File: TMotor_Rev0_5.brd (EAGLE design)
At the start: 106.7 x 79.4 mm, 105 parts, among them U1 INA125U, U10 DEV-16771, U2 INA125U, U3 INA125U, U4 INA125U, U5 SN65HVD230MDREP, U6 2SJ305TE85LF, U7 2SJ305TE85LF, U8 2SJ305TE85LF, U9 2SJ305TE85LF

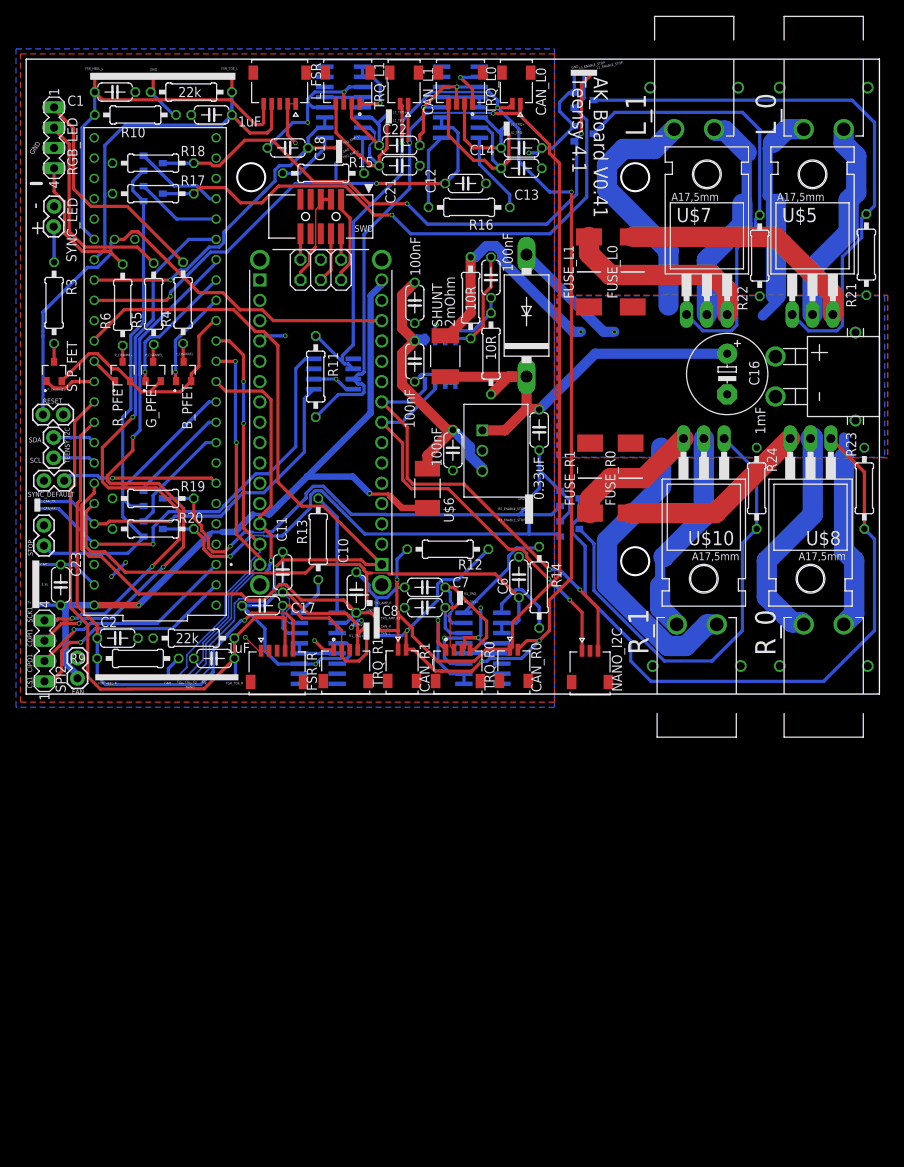
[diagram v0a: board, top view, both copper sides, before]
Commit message: Removed Power FETS, power FET supporting hardware, and SWD IO for nano
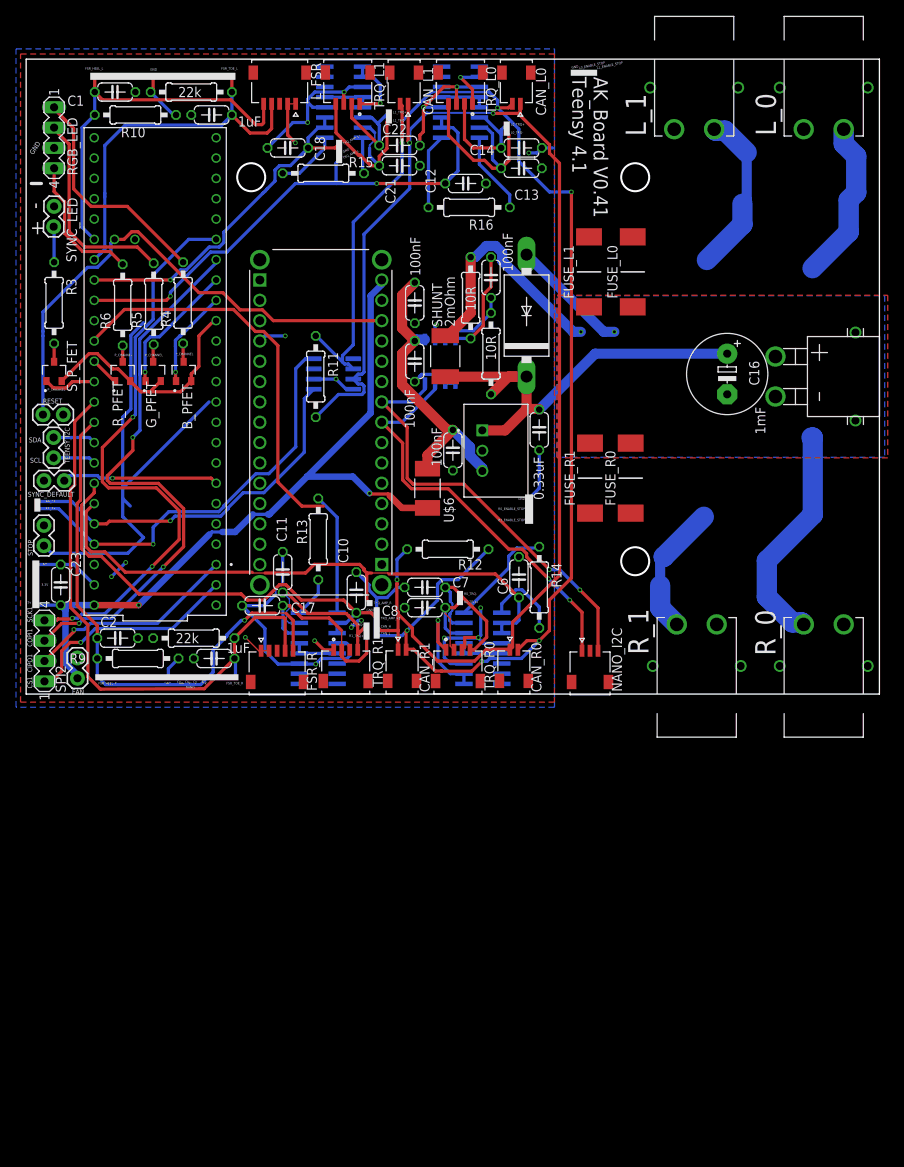
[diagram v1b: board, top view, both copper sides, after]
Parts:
- removed POGO: (no value), pinhead:2X03
- removed R17, R18: 1K, rcl:0207/10
- removed R19, R20: 1k, rcl:0207/10
- removed R21, R22, R23, R24: 10K, rcl:0207/10
- removed SWD: 20317, microbuilder:2X05_1.27MM_BOX_POSTS
- removed U$1, U$2, U$3, U$4: SSM3K329R, SnapEDA-Library:TRANS_SSM3J325F,LF
- removed U$10, U$5, U$7, U$8: FQP12P20, SnapEDA-Library:TO220
- removed U6, U7, U8, U9: 2SJ305TE85LF, 2SJ305TE85LF:TRANS_SSM3J325F,LF
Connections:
- removed net L0_ENABLE_STOP: R17.2, U$1.1, U6.3
- removed net L1_ENABLE_STOP: R18.2, U$2.1, U7.3
- removed net L_0_ENABLE: U10.28, U6.2
- removed net L_1_ENABLE: U10.29, U7.2
- removed net MISO: U10.11, USB.B15
- removed net MOSI: U10.12, USB.B14
- removed net N$43: R21.2, U$1.3, U$5.1
- removed net N$46: FUSE_R1.2, U$10.3
- removed net N$47: R23.2, U$3.3, U$8.1
- removed net N$48: R22.2, U$2.3, U$7.1
- removed net N$49: R24.2, U$10.1, U$4.3
- removed net N$50: FUSE_R0.2, U$8.3
- removed net N$51: FUSE_L1.2, U$7.3
- removed net N$52: FUSE_L0.2, U$5.3
- removed net NANO_CS: U10.10, USB.B13
- removed net NRESET: POGO.5, SWD.10
- removed net R0_ENABLE_STOP: R19.2, U$3.1, U8.3
- removed net R1_ENABLE_STOP: R20.2, U$4.1, U9.3
- removed net R_0_ENABLE: U10.8, U8.2
- removed net R_1_ENABLE: U10.7, U9.2
- removed net SW3.3V: POGO.2, SWD.1
- removed net SWCLK: POGO.4, SWD.4
- removed net SWDIO: POGO.1, SWD.2
- removed net SWGND: POGO.6, SWD.3, SWD.5
- net GND: no longer R17.1, R18.1, R19.1, R20.1, U$1.2, U$2.2, U$3.2, U$4.2
- net N$53: now also FUSE_L0.2; no longer U$5.2
- net N$54: now also FUSE_L1.2; no longer U$7.2
- net N$55: now also FUSE_R0.2; no longer U$8.2
- net N$56: now also FUSE_R1.2; no longer U$10.2
- net SCK: no longer USB.A1
- net STOP: no longer U10.9, U6.1, U7.1, U8.1, U9.1
- net VCC: no longer R21.1, R22.1, R23.1, R24.1
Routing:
- net GND: track 306.0 -> 164.2 mm, vias 24 -> 23
- net N$47: track 84.1 -> 0.00 mm
- net L0_ENABLE_STOP: track 76.0 -> 0.00 mm, vias 2 -> 0
- net L1_ENABLE_STOP: track 75.4 -> 0.00 mm, vias 3 -> 0
- net N$43: track 70.7 -> 0.00 mm
- net R0_ENABLE_STOP: track 62.2 -> 0.00 mm, vias 2 -> 0
- net R1_ENABLE_STOP: track 60.3 -> 0.00 mm, vias 2 -> 0
- net N$49: track 58.7 -> 0.00 mm
- net N$48: track 55.8 -> 0.00 mm
- net MOSI: track 49.6 -> 0.00 mm, vias 3 -> 0
- net NANO_CS: track 48.4 -> 0.00 mm, vias 2 -> 0
- net MISO: track 47.2 -> 0.00 mm, vias 3 -> 0
- net SCK: track 94.7 -> 50.6 mm, vias 2 -> 0
- net N$52: track 30.5 -> 0.00 mm
- net N$51: track 24.3 -> 0.00 mm
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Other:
- board text added: "3. Remove SPI, replace with Serial and I2C between boards"
- board text removed: "3. Figure out how to keep SPI from preventing flashing"

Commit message: Added serial connection between nano and teensy
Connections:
- new net NANO_RX: U10.35, USB.B2
- new net NANO_TX: U10.34, USB.B1
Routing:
- net N$54: track 20.8 -> 0.00 mm
- net N$53: track 20.3 -> 0.00 mm
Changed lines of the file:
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@@
 <wire x1="47.3475" y1="75.368" x2="63.54" y2="75.368" width="0" layer="19" extent="1-1"/>
 <wire x1="32.14" y1="73.025" x2="47.3475" y2="75.368" width="0" layer="19" extent="16-16"/>
-<wire x1="30.7975" y1="70.485" x2="29.1747" y2="72.4027875" width="0" layer="19" extent="1-1"/>
-<wire x1="23.8125" y1="68.58" x2="29.1747" y2="72.4027875" width="0" layer="19" extent="1-1"/>
-<wire x1="15.5575" y1="70.8025" x2="23.8125" y2="68.58" width="0" layer="19" extent="1-1"/>
-<wire x1="15.5575" y1="73.3425" x2="15.5575" y2="70.8025" width="0" layer="19" extent="1-1"/>
-<wire x1="8.3947" y1="80.645" x2="16.002" y2="78.105" width="0" layer="19" extent="16-16"/>
-<wire x1="5.461" y1="72.517" x2="1.524" y2="76.2" width="0" layer="19" extent="1-1"/>
-<wire x1="28.8925" y1="59.69" x2="23.8125" y2="68.58" width="0" layer="19" extent="1-1"/>
-<wire x1="-13.0175" y1="77.1525" x2="-3.4925" y2="73.025" width="0" layer="19" extent="1-1"/>
-<wire x1="-14.9225" y1="77.1525" x2="-13.0175" y2="77.1525" width="0" layer="19" extent="1-1"/>
-<wire x1="-20.0025" y1="80.01" x2="-18.0975" y2="80.01" width="0" layer="19" extent="1-1"/>
-<wire x1="-30.1625" y1="73.025" x2="-20.0025" y2="80.01" width="0" layer="19" extent="1-1"/>
-<wire x1="-30.1625" y1="65.7225" x2="-30.1625" y2="73.025" width="0" layer="19" extent="1-1"/>
-<wire x1="17.6431" y1="50.9496" x2="28.8925" y2="59.69" width="0" layer="19" extent="1-1"/>
-<wire x1="14.9225" y1="51.1175" x2="17.6431" y2="50.9496" width="0" layer="19" extent="1-1"/>
-<wire x1="10.795" y1="53.975" x2="14.9225" y2="51.1175" width="0" layer="19" extent="1-1"/>
-<wire x1="18.7325" y1="43.63085" x2="17.4625" y2="49.07915" width="0" layer="19" extent="16-16"/>
-<wire x1="7.2325" y1="42.8625" x2="14.9225" y2="43.815" width="0" layer="19" extent="16-16"/>
-<wire x1="-1.27" y1="49.53" x2="2.2925" y2="44.1325" width="0" layer="19" extent="16-16"/>
-<wire x1="23.368" y1="35.179" x2="20.0025" y2="43.63085" width="0" layer="19" extent="16-16"/>
-<wire x1="19.685" y1="32.7025" x2="23.368" y2="35.179" width="0" layer="19" extent="1-1"/>
-<wire x1="30.48" y1="35.2425" x2="23.368" y2="35.179" width="0" layer="19" extent="1-1"/>
-<wire x1="27.94" y1="21.9075" x2="29.21" y2="29.21" width="0" layer="19" extent="1-1"/>
-<wire x1="23.163796875" y1="15.543796875" x2="27.94" y2="21.9075" width="0" layer="19" extent="1-1"/>
-<wire x1="13.6525" y1="15.5575" x2="18.6189875" y2="11.775" width="0" layer="19" extent="1-1"/>
-<wire x1="13.6525" y1="18.0975" x2="13.6525" y2="15.5575" width="0" layer="19" extent="1-1"/>
-<wire x1="8.255" y1="13.97" x2="10.16" y2="15.24" width="0" layer="19" extent="1-1"/>
-<wire x1="5.2197" y1="11.1125" x2="6.985" y2="13.081" width="0" layer="19" extent="16-16"/>
-<wire x1="6.7865" y1="10.287" x2="5.2197" y2="11.1125" width="0" layer="19" extent="1-16"/>
-<wire x1="-9.906" y1="15.875" x2="-6.6675" y2="15.8115" width="0" layer="19" extent="1-1"/>
-<wire x1="-12.7" y1="9.2075" x2="-9.906" y2="15.875" width="0" layer="19" extent="1-1"/>
-<wire x1="-14.605" y1="9.2075" x2="-12.7" y2="9.2075" width="0" layer="19" extent="1-1"/>
-<wire x1="-17.78" y1="11.7475" x2="-14.605" y2="9.2075" width="0" layer="19" extent="1-1"/>
-<wire x1="-19.685" y1="11.7475" x2="-17.78" y2="11.7475" width="0" layer="19" extent="1-1"/>
-<wire x1="-27.2415" y1="9.271" x2="-19.685" y2="11.7475" width="0" layer="19" extent="1-1"/>
-<wire x1="-22.987" y1="19.431" x2="-19.685" y2="11.7475" width="0" layer="19" extent="1-1"/>
-<wire x1="-25.146" y1="18.415" x2="-22.987" y2="19.431" width="0" layer="19" extent="1-1"/>
-<wire x1="-31.4325" y1="25.8445" x2="-32.512" y2="20.955" width="0" layer="19" extent="1-1"/>
-<wire x1="-31.4325" y1="31.4325" x2="-31.4325" y2="25.8445" width="0" layer="19" extent="1-1"/>
-<wire x1="-29.0195" y1="39.6875" x2="-31.4325" y2="31.4325" width="0" layer="19" extent="1-1"/>
-<wire x1="-25.146" y1="51.435" x2="-29.0195" y2="39.6875" width="0" layer="19" extent="1-1"/>
-<wire x1="53.975" y1="42.2275" x2="39.878" y2="50.038" width="0" layer="19" extent="1-1"/>
-<wire x1="60.0075" y1="41.95" x2="53.975" y2="42.2275" width="0" layer="19" extent="1-1"/>
 <wire x1="52.665" y1="13.4685" x2="27.94" y2="21.9075" width="0" layer="19" extent="1-1"/>
 <wire x1="68.54" y1="13.4685" x2="52.665" y2="13.4685" width="0" layer="19" extent="1-1"/>
@@
 <wire x1="18.7325" y1="49.5554" x2="19.0246" y2="49.5554" width="0.4064" layer="1"/>
 <wire x1="19.0246" y1="49.5554" x2="19.05" y2="49.53" width="0.4064" layer="1"/>
-<wire x1="42.164" y1="53.156" x2="60.0075" y2="46.95" width="0" layer="19" extent="1-1"/>
-<wire x1="36.703" y1="53.156" x2="42.164" y2="53.156" width="0" layer="19" extent="1-1"/>
-<wire x1="35.687" y1="50.038" x2="36.703" y2="53.156" width="0" layer="19" extent="1-1"/>
-<wire x1="36.83" y1="36.125" x2="35.687" y2="50.038" width="0" layer="19" extent="1-1"/>
-<wire x1="41.91" y1="36.125" x2="36.83" y2="36.125" width="0" layer="19" extent="1-1"/>
 </signal>
 <signal name="N$23">
@@
 <signal name="N$53">
 <contactref element="L_0" pad="+"/>
-<wire x1="70.104" y1="67.460975" x2="70.104" y2="71.985025" width="2.54" layer="16"/>
-<wire x1="69.1624" y1="66.519375" x2="70.104" y2="67.460975" width="2.54" layer="16"/>
-<wire x1="70.104" y1="71.985025" x2="68.54" y2="73.549025" width="2.54" layer="16"/>
-<wire x1="68.54" y1="73.549025" x2="68.54" y2="75.368" width="2.54" layer="16"/>
-<wire x1="69.1624" y1="62.510825" x2="69.1624" y2="66.519375" width="2.54" layer="16"/>
-<wire x1="64.643" y1="57.991425" x2="69.1624" y2="62.510825" width="2.54" layer="16"/>
 <contactref element="FUSE_L0" pad="2"/>
-<wire x1="42.164" y1="61.906" x2="64.643" y2="57.991425" width="0" layer="19" extent="1-16"/>
+<wire x1="42.164" y1="61.906" x2="68.54" y2="75.368" width="0" layer="19" extent="1-1"/>
 </signal>
 <signal name="N$54">
 <contactref element="L_1" pad="+"/>
-<wire x1="52.3475" y1="75.368" x2="52.5315" y2="75.184" width="2.54" layer="16"/>
-<wire x1="52.5315" y1="75.184" x2="53.697025" y2="75.184" width="2.54" layer="16"/>
-<wire x1="53.697025" y1="75.184" x2="56.4134" y2="72.467625" width="2.54" layer="16"/>
-<wire x1="55.88" y1="66.04" x2="55.88" y2="63.46145" width="2.54" layer="16"/>
-<wire x1="51.435" y1="59.01645" x2="55.88" y2="63.46145" width="2.54" layer="16"/>
-<wire x1="56.4134" y1="72.467625" x2="56.4134" y2="66.5734" width="1.27" layer="16"/>
-<wire x1="56.4134" y1="66.5734" x2="55.88" y2="66.04" width="1.27" layer="16"/>
 <contactref element="FUSE_L1" pad="2"/>
-<wire x1="36.703" y1="61.906" x2="51.435" y2="59.01645" width="0" layer="19" extent="1-16"/>
+<wire x1="36.703" y1="61.906" x2="52.3475" y2="75.368" width="0" layer="19" extent="1-1"/>
 </signal>
 <signal name="N$55">
@@
 <wire x1="-31.369" y1="6.35" x2="-30.48" y2="6.35" width="0.4064" layer="1"/>
 </signal>
+<signal name="NANO_RX">
+<contactref element="USB" pad="B2"/>
+<contactref element="U10" pad="35"/>
+<wire x1="-25.146" y1="69.215" x2="-4.445" y2="53.975" width="0" layer="19" extent="1-1"/>
+</signal>
+<signal name="NANO_TX">
+<contactref element="USB" pad="B1"/>
+<contactref element="U10" pad="34"/>
+<wire x1="-25.146" y1="71.755" x2="-4.445" y2="56.515" width="0" layer="19" extent="1-1"/>
+</signal>
 </signals>

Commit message: Added Upright Power connectors
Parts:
- removed FUSE_R0, FUSE_R1: 0456020.ER, SamacSys_Parts:FUSC10131X312N
- removed L_0, L_1, R_0, R_1: XT30PW-F, XT30PW-M:XT30PWF
- removed U$9: XT30, Ben_Library:XT30_HORIZONTAL
- added FUSE_L2, FUSE_L3: 0456020.ER, SamacSys_Parts:FUSC10131X312N
- added XT30UPB-F, XT30UPB-F1, XT30UPB-F2, XT30UPB-F3, XT30UPB-F4: L_0, XT30UPB-F:XT30UPB-F
- moved FUSE_L1 105.9 mm to (-29.2, -25.4), turned to 0 degrees
- moved C16 15.2 mm to (38.7, 44.8)
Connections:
- removed net N$54: FUSE_L1.2, L_1.+
- removed net N$55: FUSE_R0.2, R_0.+
- removed net N$56: FUSE_R1.2, R_1.+
- new net N$43: FUSE_L1.2
- new net N$46: FUSE_L2.2
- new net N$47: FUSE_L3.2
- new net VCC1: FUSE_L1.1
- new net VCC2: FUSE_L2.1
- new net VCC3: FUSE_L3.1
- net GND: no longer L_0.-, L_1.-, R_0.-, R_1.-, U$9.-
- net N$53: no longer L_0.+
- net VCC: no longer FUSE_L1.1, FUSE_R0.1, FUSE_R1.1, U$9.+
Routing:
- net N$55: track 28.5 -> 0.00 mm
- net N$56: track 16.6 -> 0.00 mm
- net L7_VIN: track 54.2 -> 39.0 mm

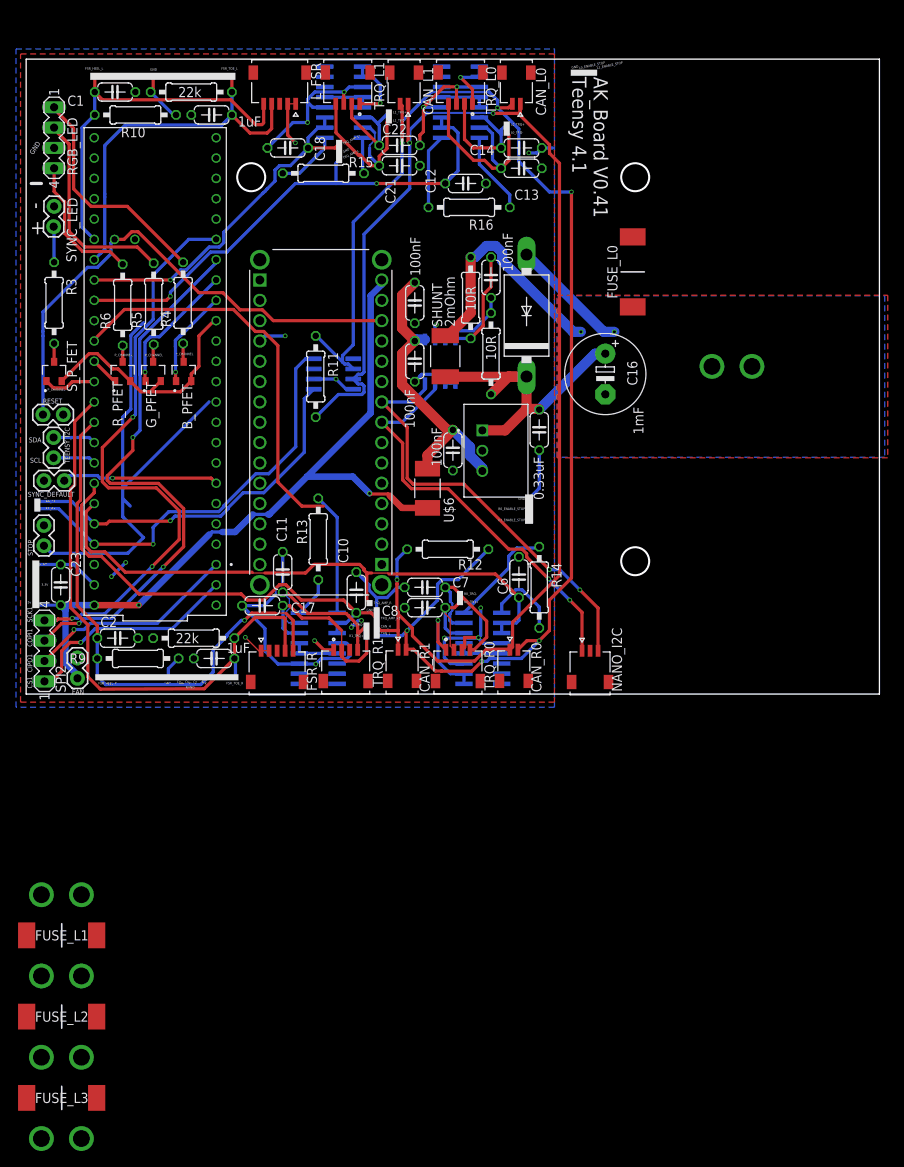
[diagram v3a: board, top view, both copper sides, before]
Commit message: Arranged new connectors
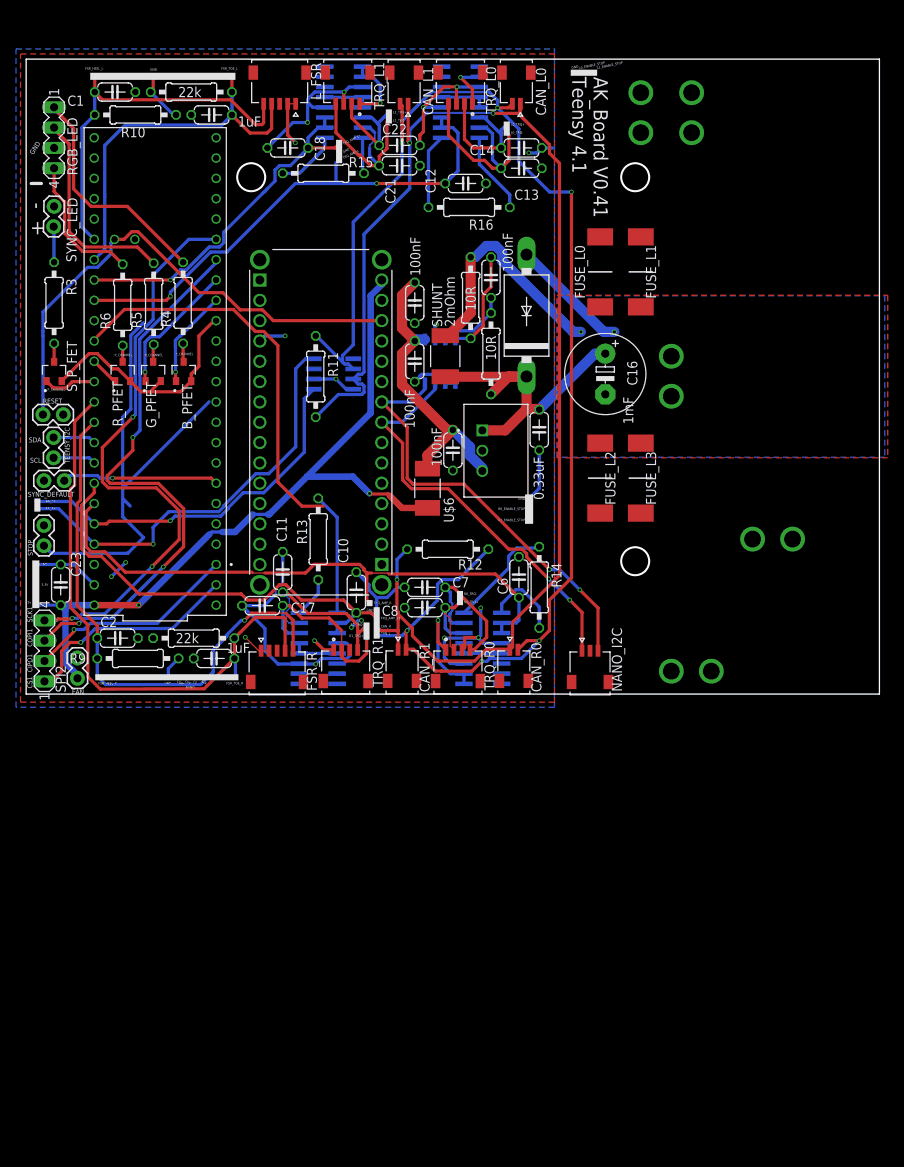
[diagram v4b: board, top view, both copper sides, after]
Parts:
- moved XT30UPB-F4 125.6 mm to (47.0, 47.0), turned to 270 degrees
- moved XT30UPB-F1 125.2 mm to (49.5, 74.9), turned to 90 degrees
- moved FUSE_L1 110.1 mm to (43.2, 57.5), turned to 90 degrees
- moved XT30UPB-F3 110.0 mm to (57.1, 24.1)
- moved FUSE_L3 106.0 mm to (43.2, 31.8), turned to 270 degrees
- moved FUSE_L2 95.2 mm to (38.1, 31.8), turned to 270 degrees
- moved XT30UPB-F2 87.5 mm to (47.0, 7.62)
- moved XT30UPB-F 30.5 mm to (43.2, 74.9), turned to 90 degrees
- moved FUSE_L0 4.06 mm to (38.1, 57.5)
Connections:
- removed net VCC: FUSE_L0.1, R2.2, SHUNT.2
- removed net VCC2: FUSE_L2.1
- removed net VCC3: FUSE_L3.1
- net GND: now also XT30UPB-F.-, XT30UPB-F1.-, XT30UPB-F2.-, XT30UPB-F3.-, XT30UPB-F4.-
- net N$43: now also XT30UPB-F1.+
- net N$46: now also XT30UPB-F2.+
- net N$47: now also XT30UPB-F3.+
- net N$53: now also XT30UPB-F.+
- net VCC1: now also FUSE_L0.1, FUSE_L2.1, FUSE_L3.1, R2.2, SHUNT.2, XT30UPB-F4.+
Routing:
- net VCC1: track 0.00 -> 30.8 mm, vias 0 -> 1
- net VCC: track 30.8 -> 0.00 mm, vias 1 -> 0
